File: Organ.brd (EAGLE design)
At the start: 97.5 x 44.4 mm, 16 parts, among them IC1 NE555

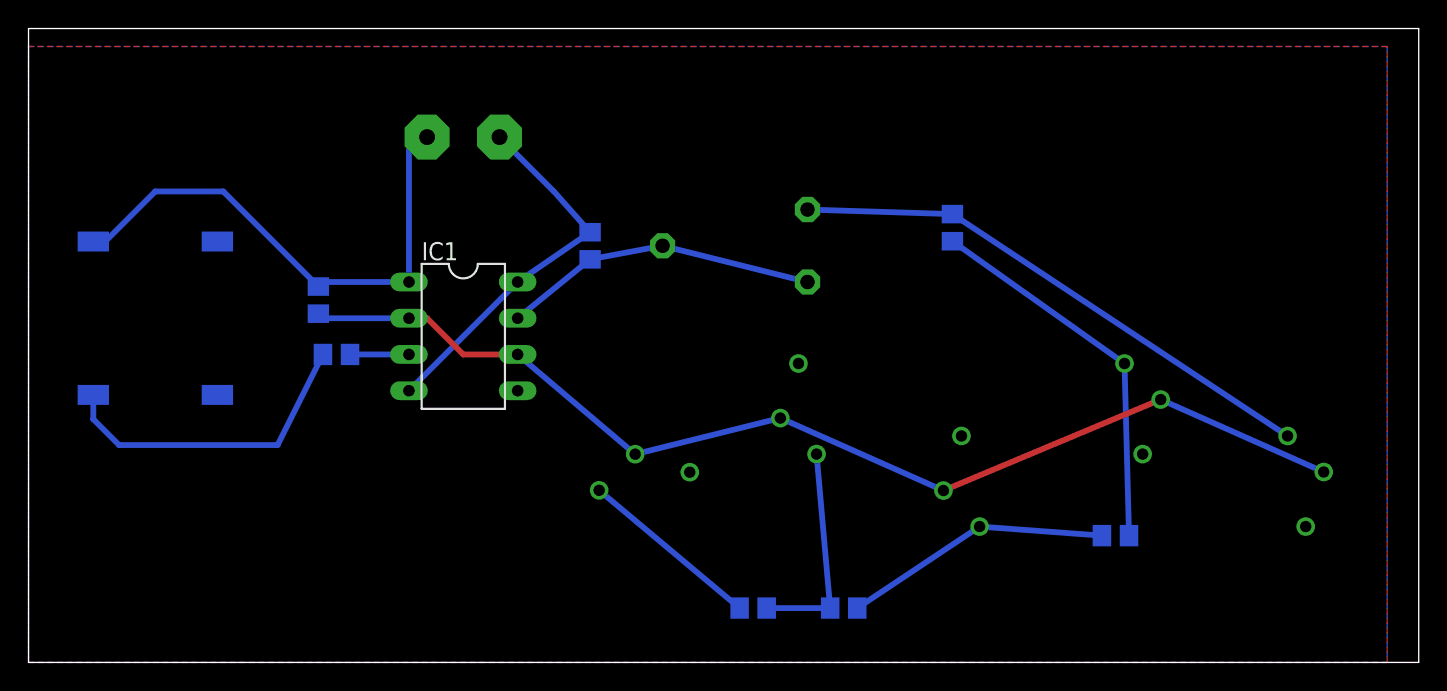
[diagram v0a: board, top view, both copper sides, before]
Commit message: Shink board footprint
Make board smaller, less costly
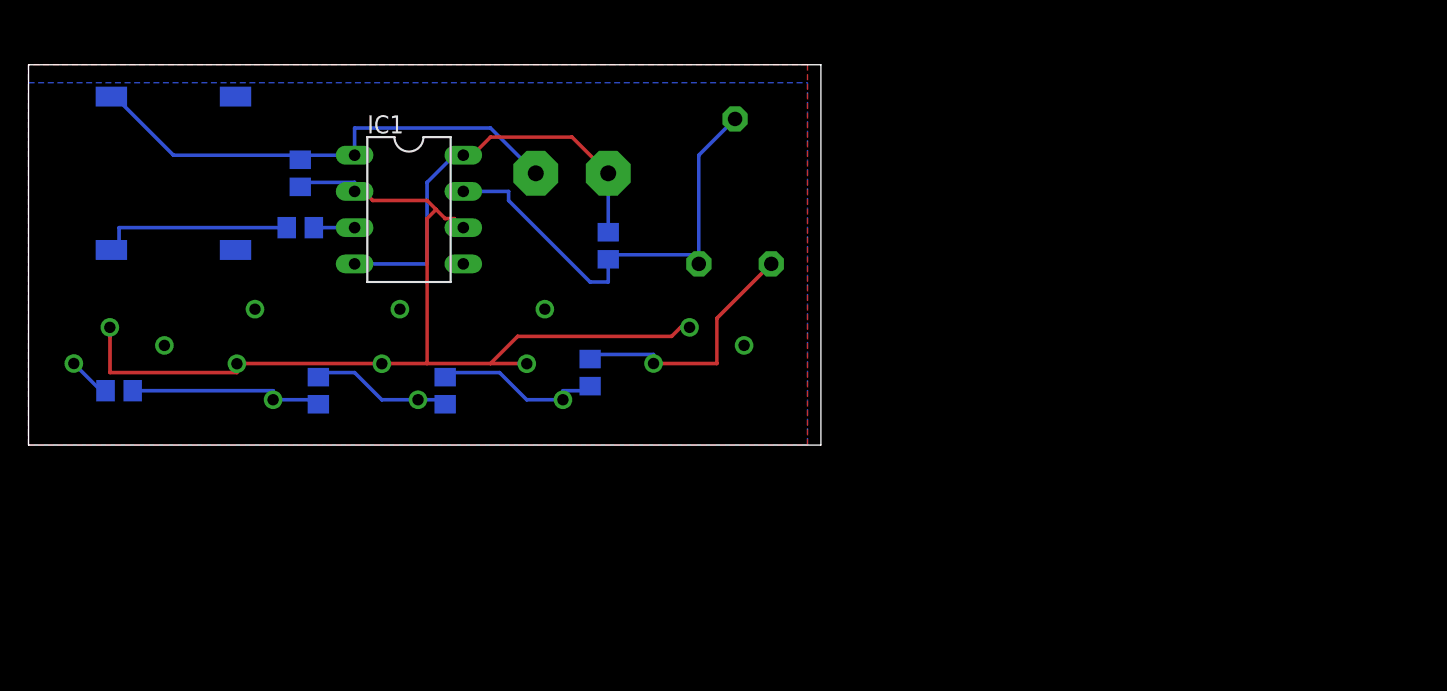
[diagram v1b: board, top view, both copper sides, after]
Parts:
- moved R3 48.1 mm to (29.2, 48.3), turned to 90 degrees
- moved R5 47.0 mm to (6.35, 48.3)
- moved S10 42.8 mm to (47.0, 50.8), turned to 0 degrees
- moved S9 40.8 mm to (36.8, 50.8), turned to 270 degrees
- moved S8 40.4 mm to (26.7, 50.8)
- moved R4 39.9 mm to (20.3, 48.3), turned to 90 degrees
- moved S6 38.3 mm to (16.5, 50.8)
- moved S7 37.9 mm to (6.35, 50.8)
- moved R2 27.4 mm to (39.4, 49.5)
- moved SP1 10.2 mm to (10.2, 63.5)
- moved IC1 9.67 mm to (26.7, 61.0)
- moved C1 9.25 mm to (19.1, 59.7)
- moved C2 8.98 mm to (19.1, 63.5)
- moved G1 8.03 mm to (38.1, 63.5)
- moved R6 3.81 mm to (49.5, 62.2), turned to 0 degrees
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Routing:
- net B5: track 38.3 -> 18.4 mm
- net B4: track 26.9 -> 12.2 mm
- net POT: track 22.2 -> 32.6 mm
- net B1: track 12.8 -> 3.01 mm
- net SIGNAL: track 22.5 -> 13.6 mm
- net B3: track 18.9 -> 10.3 mm
- net DISCHARGE: track 78.0 -> 72.5 mm
- net VCC: track 26.2 -> 30.0 mm
- net GROUND: track 37.9 -> 34.9 mm
- net B2: track 15.3 -> 14.0 mm
- net N$11: track 4.13 -> 2.86 mm
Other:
- board size 97.5 x 44.4 mm -> 55.5 x 26.7 mm
